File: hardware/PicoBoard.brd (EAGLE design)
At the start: 110.5 x 59.1 mm, 44 parts, among them J1 AVR Prog., U1 FT232RLSSOP, U10 SLIDER, U2 ATMEGA328, U3 2.5mm, U4 2.5mm, U5 2.5mm, U6 2.5mm, U7 TEMT6000, U8 LMV358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

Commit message: Re-Up
The New REV somehow was lost, now it is not.
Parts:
- moved LED2 0.77 mm to (44.5, 44.5)
- moved R2 0.51 mm to (44.5, 45.7)
- moved R1 0.25 mm to (40.6, 45.7)
- moved LED1 0.13 mm to (40.6, 44.5)
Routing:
- net RXLED: track 5.96 -> 5.32 mm
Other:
- board text added: "v1"
- board text removed: "v11"
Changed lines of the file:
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@@
 <layer number="27" name="tValues" color="7" fill="1" visible="no" active="yes"/>
 <layer number="28" name="bValues" color="7" fill="1" visible="no" active="yes"/>
-<layer number="29" name="tStop" color="7" fill="3" visible="no" active="yes"/>
+<layer number="29" name="tStop" color="7" fill="3" visible="yes" active="yes"/>
 <layer number="30" name="bStop" color="7" fill="6" visible="no" active="yes"/>
 <layer number="31" name="tCream" color="7" fill="4" visible="no" active="yes"/>
@@
 <layer number="106" name="bPlate" color="7" fill="1" visible="no" active="yes"/>
 <layer number="107" name="Crop" color="7" fill="1" visible="no" active="yes"/>
-<layer number="108" name="tplace-old" color="10" fill="1" visible="no" active="yes"/>
-<layer number="109" name="ref-old" color="11" fill="1" visible="no" active="yes"/>
+<layer number="108" name="tplace-old" color="10" fill="1" visible="yes" active="yes"/>
+<layer number="109" name="ref-old" color="11" fill="1" visible="yes" active="yes"/>
 <layer number="116" name="Patch_BOT" color="9" fill="4" visible="no" active="yes"/>
 <layer number="121" name="_tsilk" color="7" fill="1" visible="no" active="yes"/>
@@
 <text x="12.065" y="34.417" size="3.81" layer="21" font="vector" ratio="15" rot="SR270">B</text>
 <text x="12.065" y="43.307" size="3.81" layer="21" font="vector" ratio="15" rot="SR270">A</text>
-<text x="57.15" y="5.08" size="1.778" layer="16" font="vector" ratio="15" rot="MR0">v11</text>
-<text x="42.799" y="42.672" size="1.016" layer="21" font="vector" ratio="15">Tx</text>
-<text x="39.878" y="42.672" size="1.016" layer="21" font="vector" ratio="15">Rx</text>
+<text x="57.15" y="5.08" size="1.778" layer="16" font="vector" ratio="15" rot="MR0">v1</text>
+<text x="42.291" y="42.672" size="1.016" layer="21" font="vector" ratio="15">Tx</text>
+<text x="39.751" y="42.672" size="1.016" layer="21" font="vector" ratio="15">Rx</text>
 </plain>
 <attributes>
@@
 <element name="C1" library="SparkFun" package="0603-CAP" value="0.1uF" x="52.07" y="45.72" rot="R180"/>
 <element name="U1" library="SparkFun" package="SSOP28DB" value="FT232RLSSOP" x="49.53" y="39.37"/>
-<element name="R1" library="SparkFun" package="0603-RES" value="1K" x="40.386" y="45.72"/>
-<element name="R2" library="SparkFun" package="0603-RES" value="1K" x="43.942" y="45.72"/>
-<element name="LED1" library="SparkFun" package="LED-0603" value="Red" x="40.64" y="44.323" rot="R270"/>
-<element name="LED2" library="SparkFun" package="LED-0603" value="Green" x="43.688" y="44.323" rot="R270"/>
+<element name="R1" library="SparkFun" package="0603-RES" value="1K" x="40.64" y="45.72"/>
+<element name="R2" library="SparkFun" package="0603-RES" value="1K" x="44.45" y="45.72"/>
+<element name="LED1" library="SparkFun" package="LED-0603" value="Red" x="40.64" y="44.45" rot="R270"/>
+<element name="LED2" library="SparkFun" package="LED-0603" value="Green" x="44.45" y="44.45" rot="R270"/>
 <element name="U2" library="SparkFun" package="TQFP32-08" value="ATMEGA328" x="48.26" y="24.13"/>
 <element name="J1" library="SparkFun" package="2X3" value="AVR Prog." x="72.39" y="44.45" rot="R180"/>
@@
 <contactref element="U1" pad="23"/>
 <contactref element="LED1" pad="C"/>
-<wire x1="41.39" y1="42.684" x2="41.39" y2="44.323" width="0.254" layer="1"/>
+<wire x1="41.39" y1="42.684" x2="41.39" y2="44.45" width="0.254" layer="1"/>
 <wire x1="41.656" y1="42.418" x2="41.39" y2="42.684" width="0.254" layer="1"/>
 <wire x1="43.18" y1="42.418" x2="41.656" y2="42.418" width="0.254" layer="1"/>
@@
 <contactref element="U1" pad="22"/>
 <contactref element="LED2" pad="C"/>
-<wire x1="49.205" y1="43.026" x2="49.205" y2="44.14" width="0.254" layer="1"/>
-<wire x1="49.205" y1="44.14" x2="49.022" y2="44.323" width="0.254" layer="1"/>
-<wire x1="49.022" y1="44.323" x2="44.438" y2="44.323" width="0.254" layer="1"/>
+<wire x1="45.2" y1="44.45" x2="49.022" y2="44.45" width="0.254" layer="1"/>
+<wire x1="49.022" y1="44.45" x2="49.205" y2="44.267" width="0.254" layer="1"/>
+<wire x1="49.205" y1="44.267" x2="49.205" y2="43.026" width="0.254" layer="1"/>
 </signal>
 <signal name="N$1">
 <contactref element="R1" pad="1"/>
 <contactref element="LED1" pad="A"/>
-<wire x1="39.89" y1="44.323" x2="39.89" y2="45.72" width="0.254" layer="1"/>
-<wire x1="39.89" y1="45.72" x2="39.536" y2="45.72" width="0.254" layer="1"/>
+<wire x1="39.89" y1="44.45" x2="39.89" y2="45.72" width="0.254" layer="1"/>
+<wire x1="39.89" y1="45.72" x2="39.79" y2="45.72" width="0.254" layer="1"/>
 </signal>
 <signal name="N$2">
 <contactref element="R2" pad="1"/>
 <contactref element="LED2" pad="A"/>
-<wire x1="42.938" y1="44.323" x2="42.938" y2="45.72" width="0.254" layer="1"/>
-<wire x1="42.938" y1="45.72" x2="43.092" y2="45.72" width="0.254" layer="1"/>
+<wire x1="43.7" y1="44.45" x2="43.7" y2="45.72" width="0.254" layer="1"/>
+<wire x1="43.7" y1="45.72" x2="43.6" y2="45.72" width="0.254" layer="1"/>
 </signal>
 <signal name="TXO">
@@
 <wire x1="20.88" y1="51.34" x2="33.75" y2="51.34" width="0.254" layer="1"/>
 <wire x1="41.91" y1="37.97" x2="41.91" y2="38.1" width="0.254" layer="1"/>
-<wire x1="40.64" y1="48.006" x2="44.792" y2="48.006" width="0.254" layer="1"/>
-<wire x1="44.792" y1="48.006" x2="69.596" y2="48.006" width="0.254" layer="1"/>
+<wire x1="40.64" y1="48.006" x2="45.3" y2="48.006" width="0.254" layer="1"/>
+<wire x1="45.3" y1="48.006" x2="69.596" y2="48.006" width="0.254" layer="1"/>
 <wire x1="69.596" y1="48.006" x2="71.12" y2="46.482" width="0.254" layer="1"/>
 <wire x1="71.12" y1="46.482" x2="71.12" y2="43.18" width="0.254" layer="1"/>
@@
 <via x="90.17" y="31.75" extent="1-16" drill="0.508"/>
 <via x="92.71" y="34.29" extent="1-16" drill="0.508"/>
+<wire x1="45.3" y1="45.72" x2="45.3" y2="48.006" width="0.254" layer="1"/>
 <wire x1="42.76" y1="35.56" x2="42.76" y2="35.98" width="0.254" layer="1"/>
 <wire x1="42.76" y1="35.98" x2="41.91" y2="36.83" width="0.254" layer="1"/>
@@
 <wire x1="40.386" y1="47.752" x2="40.386" y2="46.736" width="0.254" layer="1"/>
 <wire x1="41.275" y1="46.736" x2="41.529" y2="46.482" width="0.254" layer="1"/>
-<wire x1="44.792" y1="45.72" x2="44.792" y2="48.006" width="0.254" layer="1"/>
-<wire x1="41.529" y1="46.482" x2="41.529" y2="46.013" width="0.254" layer="1"/>
-<wire x1="41.529" y1="46.013" x2="41.236" y2="45.72" width="0.254" layer="1"/>
+<wire x1="41.529" y1="46.482" x2="41.529" y2="45.759" width="0.254" layer="1"/>
+<wire x1="41.529" y1="45.759" x2="41.49" y2="45.72" width="0.254" layer="1"/>
 </signal>
 <signal name="N$5">
@@
 <wire x1="49.149" y1="27.051" x2="49.46" y2="27.362" width="0.254" layer="1"/>
 <wire x1="47.117" y1="27.051" x2="49.149" y2="27.051" width="0.254" layer="1"/>
+<wire x1="7.457" y1="30.77" x2="7.493" y2="30.734" width="0.254" layer="1"/>
+<wire x1="7.493" y1="30.734" x2="7.529" y2="30.77" width="0.254" layer="1"/>
 <via x="47.117" y="27.051" extent="1-16" drill="0.508"/>
 <via x="17.018" y="29.972" extent="1-16" drill="0.508"/>
@@
 <wire x1="11.43" y1="30.568" x2="7.2582" y2="30.568" width="0.254" layer="1"/>
 <wire x1="7.2582" y1="30.568" x2="7.2192" y2="30.607" width="0.254" layer="1"/>
+<wire x1="7.2582" y1="30.568" x2="7.457" y2="30.77" width="0" layer="19" extent="1-1"/>
 </signal>
 <signal name="RC">
@@
 <wire x1="18.542" y1="26.162" x2="33.909" y2="26.162" width="0.254" layer="16"/>
 <wire x1="17.78" y1="25.4" x2="18.542" y2="26.162" width="0.254" layer="16"/>
+<wire x1="7.584" y1="21.88" x2="7.62" y2="21.844" width="0.254" layer="1"/>
+<wire x1="7.62" y1="21.844" x2="7.656" y2="21.88" width="0.254" layer="1"/>
 <via x="33.909" y="26.162" extent="1-16" drill="0.508"/>
 <via x="17.78" y="25.4" extent="1-16" drill="0.508"/>
 <wire x1="11.43" y1="21.932" x2="14.898" y2="25.4" width="0.254" layer="1"/>
 <wire x1="14.898" y1="25.4" x2="17.78" y2="25.4" width="0.254" layer="1"/>
-<wire x1="11.43" y1="21.932" x2="7.5612" y2="21.932" width="0.254" layer="1"/>
-<wire x1="7.5612" y1="21.932" x2="7.2192" y2="21.59" width="0.254" layer="1"/>
+<wire x1="11.43" y1="21.932" x2="11.378" y2="21.88" width="0.254" layer="1"/>
+<wire x1="11.378" y1="21.88" x2="7.5092" y2="21.88" width="0.254" layer="1"/>
+<wire x1="7.5092" y1="21.88" x2="7.2192" y2="21.59" width="0.254" layer="1"/>
+<wire x1="7.5092" y1="21.88" x2="7.584" y2="21.88" width="0" layer="19" extent="1-1"/>
 </signal>
 <signal name="RD">
@@
 <wire x1="23.368" y1="24.765" x2="47.117" y2="24.765" width="0.254" layer="16"/>
 <wire x1="19.685" y1="21.082" x2="23.368" y2="24.765" width="0.254" layer="16"/>
+<wire x1="7.275" y1="12.99" x2="7.239" y2="12.954" width="0.254" layer="1"/>
 <via x="49.53" y="25.4" extent="1-16" drill="0.508"/>
 <via x="19.685" y="21.082" extent="1-16" drill="0.508"/>
@@
 <wire x1="11.43" y1="13.296" x2="10.707" y2="12.573" width="0.254" layer="1"/>
 <wire x1="10.707" y1="12.573" x2="7.2192" y2="12.573" width="0.254" layer="1"/>
+<wire x1="7.2192" y1="12.573" x2="7.239" y2="12.954" width="0" layer="19" extent="1-1"/>
 </signal>
 <signal name="SOUND">

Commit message: Re- Up
95% of the orginal Rev files we're lost, updated the lost files.
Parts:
- S2: device SparkFun:TACTILE-PTH-12MM -> SparkFun-Electromechanical:TACTILE-SMD-12MM
- U10: value SLIDER -> (none); device SparkFun:SLIDER -> SparkFun-Electromechanical:SLIDER
- U3, U4, U5, U6: device Testing:STEREOJACKSMD1:1 -> SparkFun-Connectors:STEREOJACK2.5MM
- moved C2 4.02 mm to (40.6, 31.8)
- moved C5 4.02 mm to (40.6, 35.6), turned to 0 degrees
- moved C11 2.54 mm to (89.0, 22.6)
- moved C7 2.54 mm to (89.0, 24.5)
- moved R4 2.54 mm to (89.0, 26.4)
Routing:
- net 5V: track 277.3 -> 280.3 mm
- net N$8: track 70.5 -> 71.5 mm
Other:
- board text added: "Jim Linblom"
- board text added: "Revised by: Patrick Alberts"
- board text added: "v12"
- board text removed: "v1"

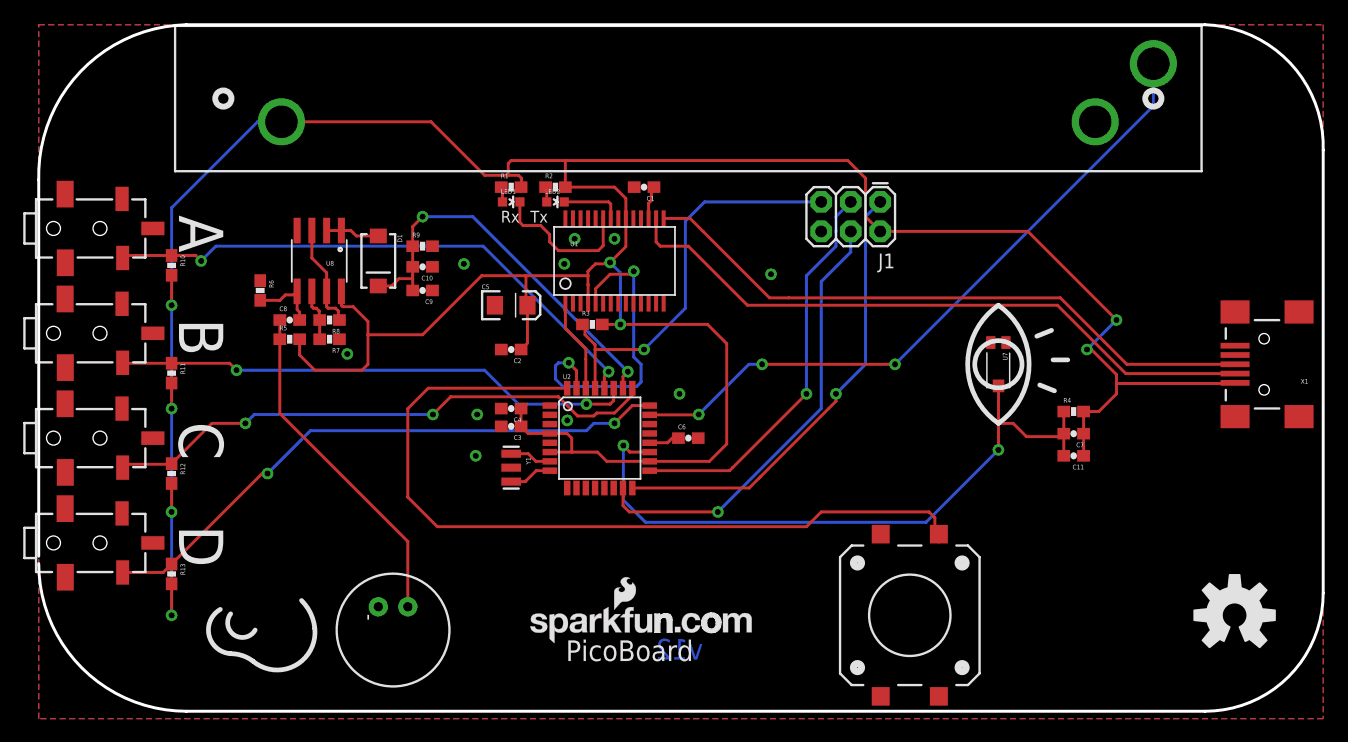
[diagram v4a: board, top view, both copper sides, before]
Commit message: Added board fiducials
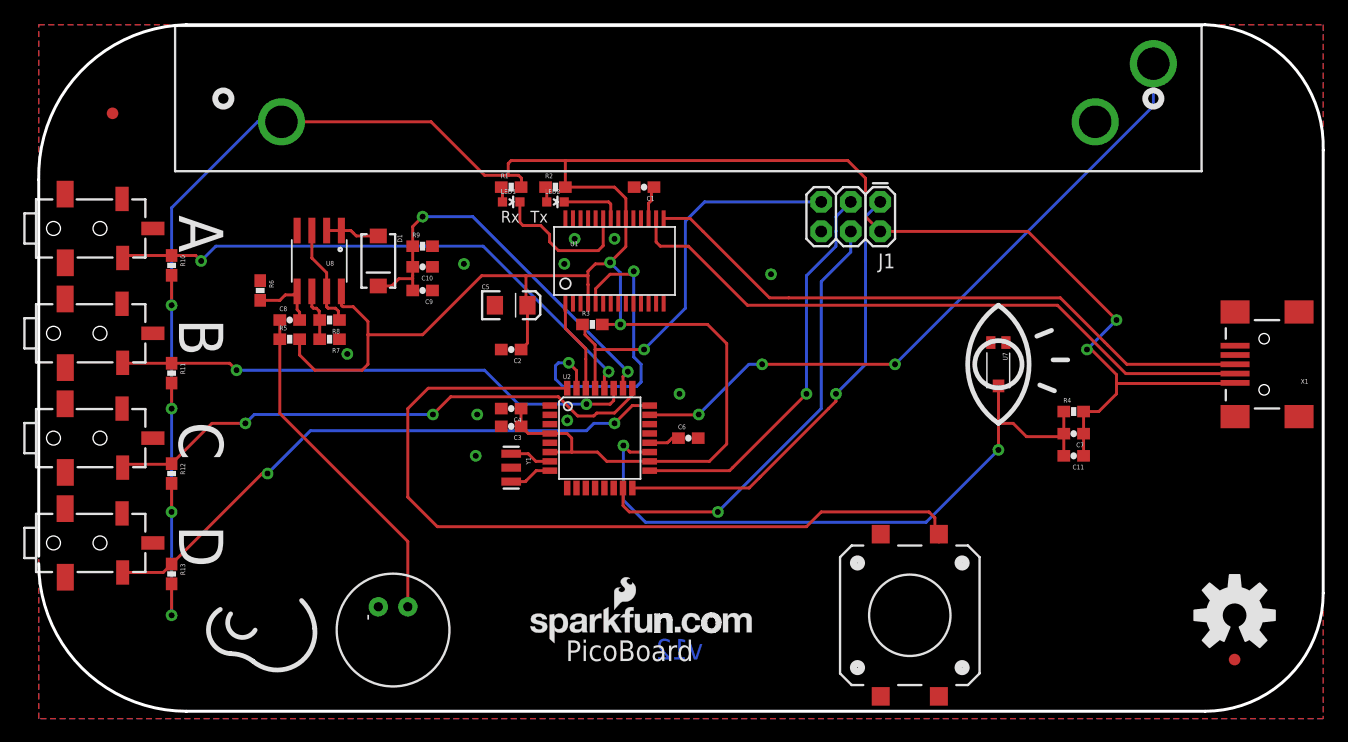
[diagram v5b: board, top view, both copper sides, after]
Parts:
- added FID1, FID2: FIDUCIAL1X2, SparkFun-Aesthetics:FIDUCIAL-1X2
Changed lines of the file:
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@@
 <?xml version="1.0" encoding="utf-8"?>
 <!DOCTYPE eagle SYSTEM "eagle.dtd">
-<eagle version="6.4">
+<eagle version="6.5.0">
 <drawing>
 <settings>
@@
 <setting verticaltext="up"/>
 </settings>
-<grid distance="0.05" unitdist="inch" unit="inch" style="lines" multiple="1" display="yes" altdistance="0.005" altunitdist="inch" altunit="inch"/>
+<grid distance="0.05" unitdist="inch" unit="inch" style="lines" multiple="1" display="yes" altdistance="0.01" altunitdist="inch" altunit="inch"/>
 <layers>
 <layer number="1" name="Top" color="4" fill="1" visible="yes" active="yes"/>
@@
 <layer number="18" name="Vias" color="2" fill="1" visible="yes" active="yes"/>
 <layer number="19" name="Unrouted" color="6" fill="1" visible="yes" active="yes"/>
-<layer number="20" name="Dimension" color="15" fill="1" visible="yes" active="yes"/>
-<layer number="21" name="tPlace" color="16" fill="1" visible="yes" active="yes"/>
-<layer number="22" name="bPlace" color="14" fill="1" visible="yes" active="yes"/>
+<layer number="20" name="Dimension" color="6" fill="1" visible="yes" active="yes"/>
+<layer number="21" name="tPlace" color="6" fill="1" visible="yes" active="yes"/>
+<layer number="22" name="bPlace" color="6" fill="1" visible="yes" active="yes"/>
 <layer number="23" name="tOrigins" color="15" fill="1" visible="yes" active="yes"/>
 <layer number="24" name="bOrigins" color="15" fill="1" visible="yes" active="yes"/>
@@
 <element name="FRAME1" library="SparkFun-Aesthetics" package="CREATIVE_COMMONS" value="FRAME-LETTER" x="20.32" y="-7.62"/>
 <element name="LOGO1" library="SparkFun-Aesthetics" package="OSHW-LOGO-L" value="OSHW-LOGOL" x="102.87" y="8.89"/>
+<element name="FID1" library="SparkFun-Aesthetics" package="FIDUCIAL-1X2" value="FIDUCIAL1X2" x="6.35" y="52.07"/>
+<element name="FID2" library="SparkFun-Aesthetics" package="FIDUCIAL-1X2" value="FIDUCIAL1X2" x="102.87" y="5.08"/>
 </elements>
 <signals>
